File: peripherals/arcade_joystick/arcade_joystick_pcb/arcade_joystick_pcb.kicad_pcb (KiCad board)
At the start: 2 copper layers, 19.1 x 22.9 mm, 6 parts, among them J1 PJ320A, J2 Mr_Joystick

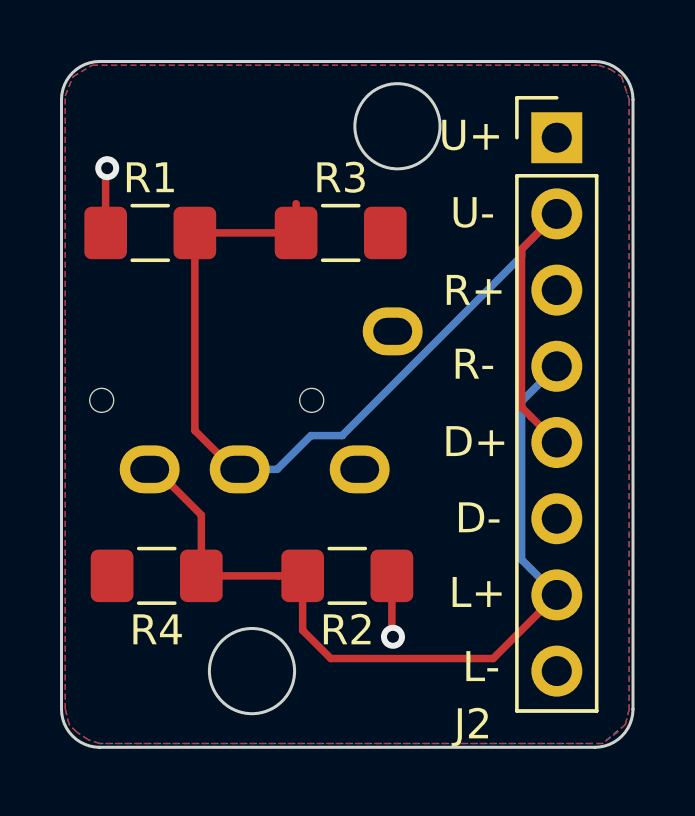
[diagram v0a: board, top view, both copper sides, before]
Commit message: Updated arcade joystick pcb design
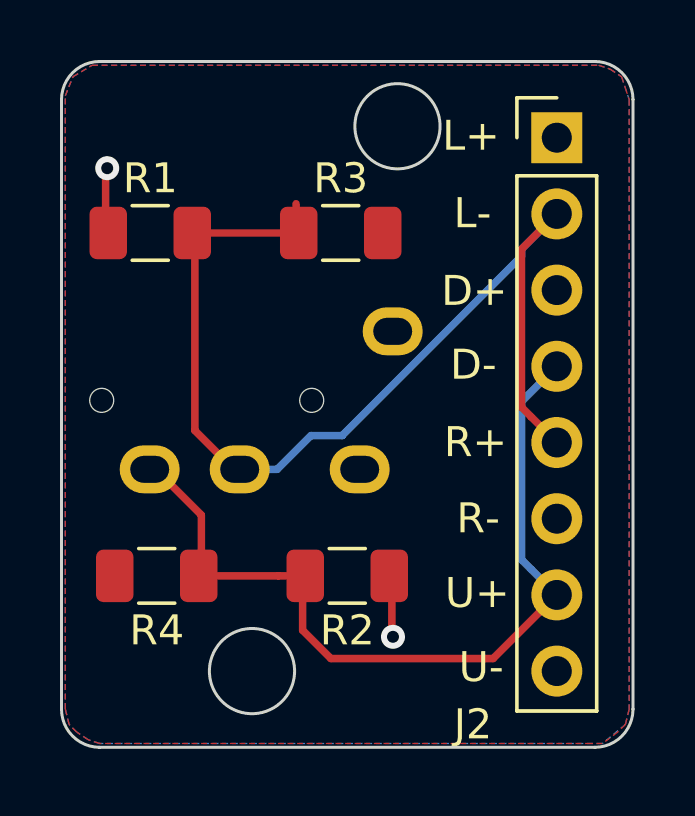
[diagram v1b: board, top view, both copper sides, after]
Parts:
- R1, R2, R3, R4: value 5k -> 10k; footprint Resistor_SMD:R_1206_3216Metric_Pad1.42x1.75mm_HandSolder -> Resistor_SMD:R_1206_3216Metric
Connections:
- net /L_R renamed /UD
- net /U_D renamed /LR
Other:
- board text added: "Arcade Joystick Interface Ver. 1.1"
- board text added: "https://github.com/ Accessible-AAC"
- board text removed: "Arcade Joystick Interface Ver. 1.0"
